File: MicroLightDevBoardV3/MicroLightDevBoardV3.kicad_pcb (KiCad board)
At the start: 6 copper layers, 12.5 x 16 mm, 33 parts, among them J1 TYPE-C-31-M-12, J3 Conn_01x03_Socket, J4 Conn_01x01_Socket, J5 Conn_01x01_Socket, J6 Conn_01x04_Socket, SW1 SW_Push, U1 USBLC6-2P6, U2 STM32C071GBUx, U3 BQ25180, U4 S-85S1AB33-I6T1U, U7 MC3479

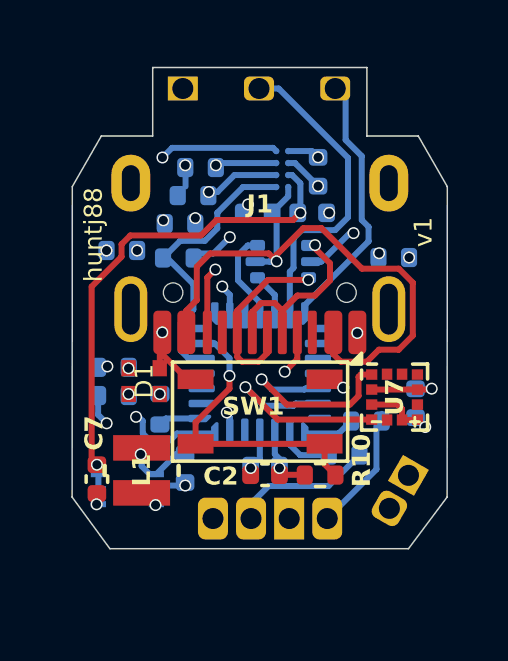
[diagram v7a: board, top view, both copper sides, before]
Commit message: Front RGB LED support via TIM3 PWM + timer refactor + PCB optimization (#19)
* updated timer and pins for integrating front rgb led

* human tasks

* human tasks

* pcb: adjust inductor and battery terminals slightly

* made dimensions exactly 12.5x14 millimeters

* pcb: optimize ground and 3.3v planes by adjusting vias

* adjust 3.3v buck position slightly

* PCB: make corners be 45 degree angles

* pcb: optimize ground plane

* pcb: optimize routing a bit

* pcb: optimize routing a bit

* pcb: optimize routing a bit

* pcb: optimize routing

* pcb: edge cut cleanup, optimize routing

* first pass at rgb led firmware

* cleaning up timers and state in rgb led firmware

* add test cases

* avoid HAL reconfigures

* cleanup

* split deps and state in chipState

* add log for corrupt mode

* cleanup

* add tests

* add click log back

* cleanup

* rename rgbTask to rgbTransientTask

* cache bulb pin state, remove redundant log and outputs

- Add writeBulbLedIfChanged() to skip redundant HAL GPIO writes
  every tick when the bulb pin state hasn't changed. Uses a 255
  sentinel so the first write always reaches hardware.
- Remove duplicate plain-text 'clicked' log, keep only the
  structured JSON modeChanged event.
- Remove meaningless frontType=BULB assignment in
  disableFrontOutputs() when frontValid is already false.
- Assert both period and prescaler match for TIM1/TIM3.

* fix bug with fBlue in rgb mode

* remove function wrapper

* cleanup

* cleanup and test

* false positive lint from HAL?

* use hardware registers to check which mode a pin is in for setting RGB PWM vs BULB GPIO

* cleanup

* cleanup

* Refactor: code review cleanup across chip_state, mode_manager, headers, and tests

- Cache getChargingState() result in stateTask to avoid redundant I2C reads
- Rename caseLedBusyWithCharge to caseLedReservedForStatus, caseLedBusyWithButton to caseLedReservedForButton
- Add early-return guard in modeTask; remove redundant NULL checks in mode_manager
- Add docume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
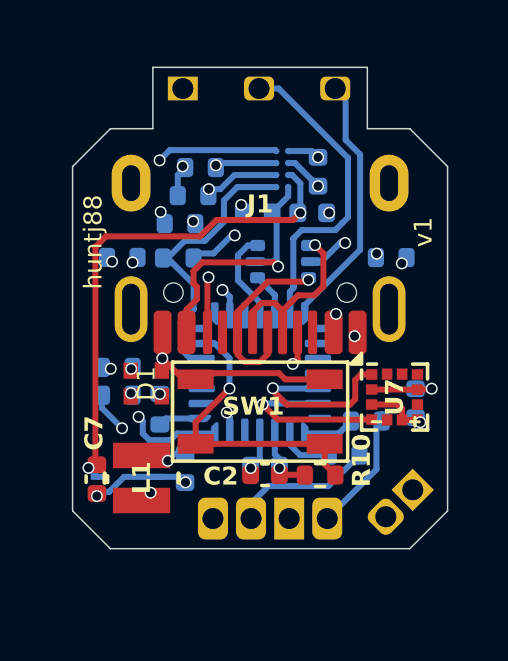
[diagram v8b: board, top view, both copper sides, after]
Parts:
- moved J5 0.50 mm to (54.8, 31.8), turned to -135 degrees
- moved U4 0.41 mm to (45.3, 31.4)
- moved J4 0.30 mm to (54.0, 32.7), turned to 135 degrees
- moved L1 0.25 mm to (45.8, 31.4)
- moved R13 0.23 mm to (45.2, 24.1)
- moved R6 0.13 mm to (45.0, 28.7)
- moved R7 0.13 mm to (45.0, 27.7)
- moved D1 0.11 mm to (46.0, 28.3)
- moved R2 0.09 mm to (54.1, 24.1)
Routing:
- net GND: track 19.4 -> 24.6 mm, vias 13 -> 12
- net VBUS_CHRG: track 20.2 -> 16.7 mm, vias 1 -> 2
- net Net-(J1-CC1): track 8.95 -> 7.30 mm
- net Net-(J6-Pin_1): track 13.6 -> 11.9 mm
- net I2C_SDA: track 18.6 -> 17.2 mm
- net TS_MR_CHRG: track 24.1 -> 23.0 mm
- net SYS_CHRG: track 16.6 -> 17.1 mm
- net Net-(J1-D--PadA7): track 6.25 -> 6.76 mm
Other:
- outline, holes or cut-outs redrawn
